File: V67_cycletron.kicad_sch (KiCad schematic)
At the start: 52 parts, among them J1 USB_C_Receptacle_USB2.0_16P, J3 Screw_Terminal_01x11, U1 LM1117DT-5.0, U2 LM1117DT-3.3, U4 ESP32-S3-WROOM-1

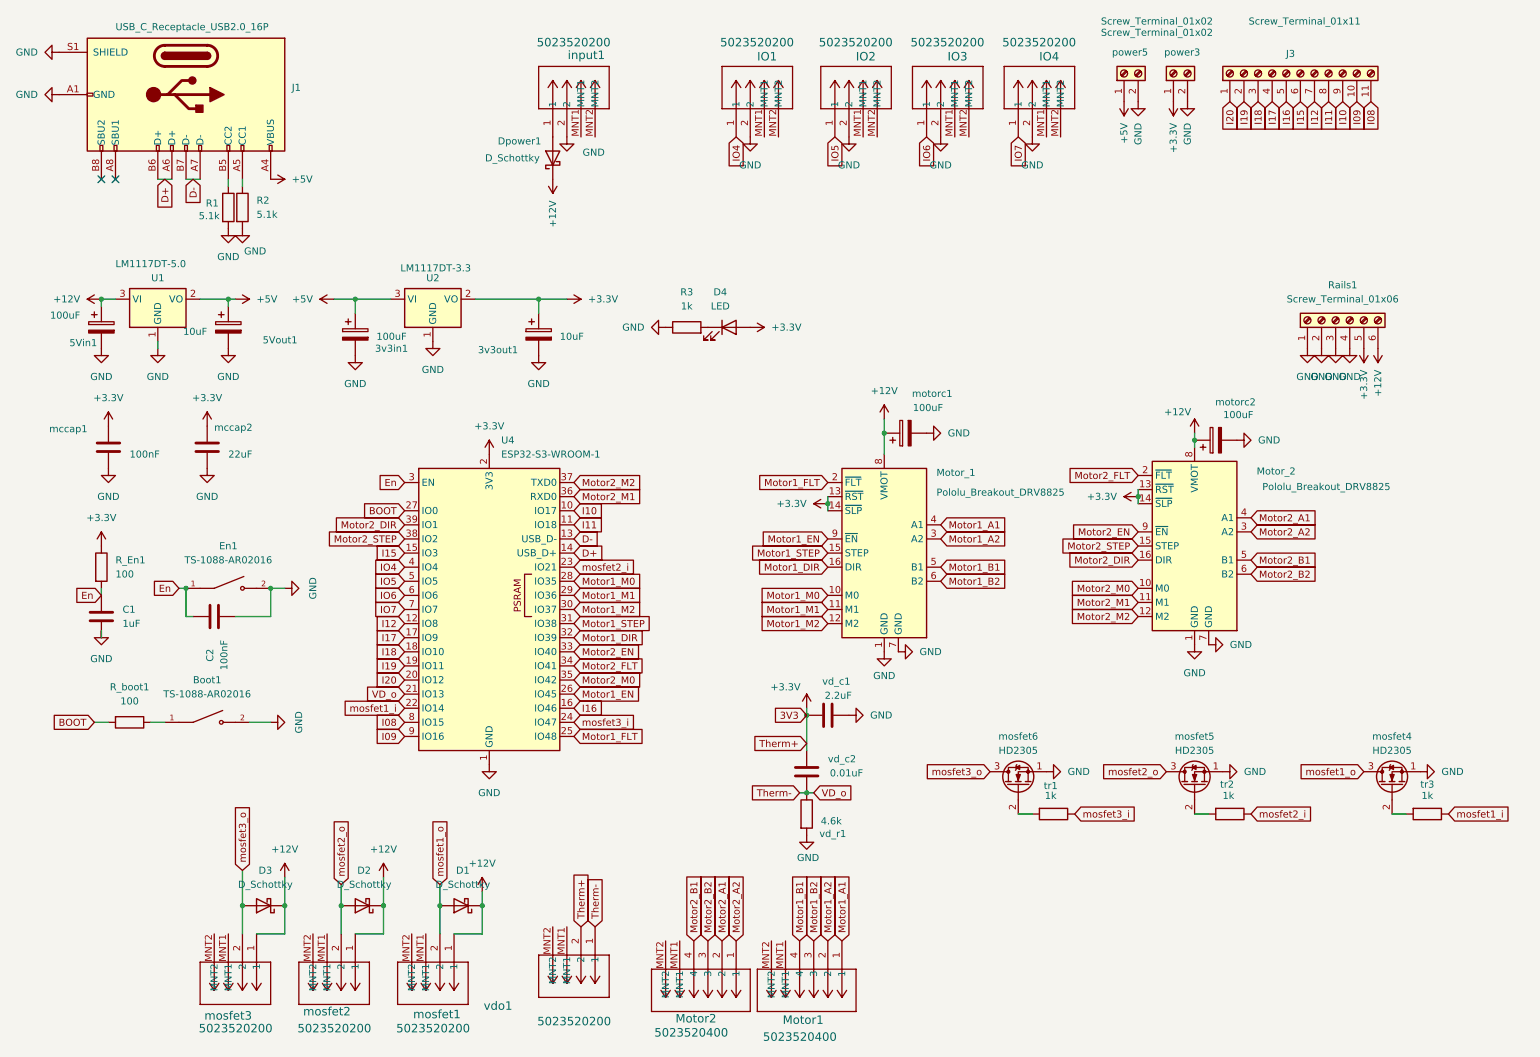
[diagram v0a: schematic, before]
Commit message: re-arranged connector positions
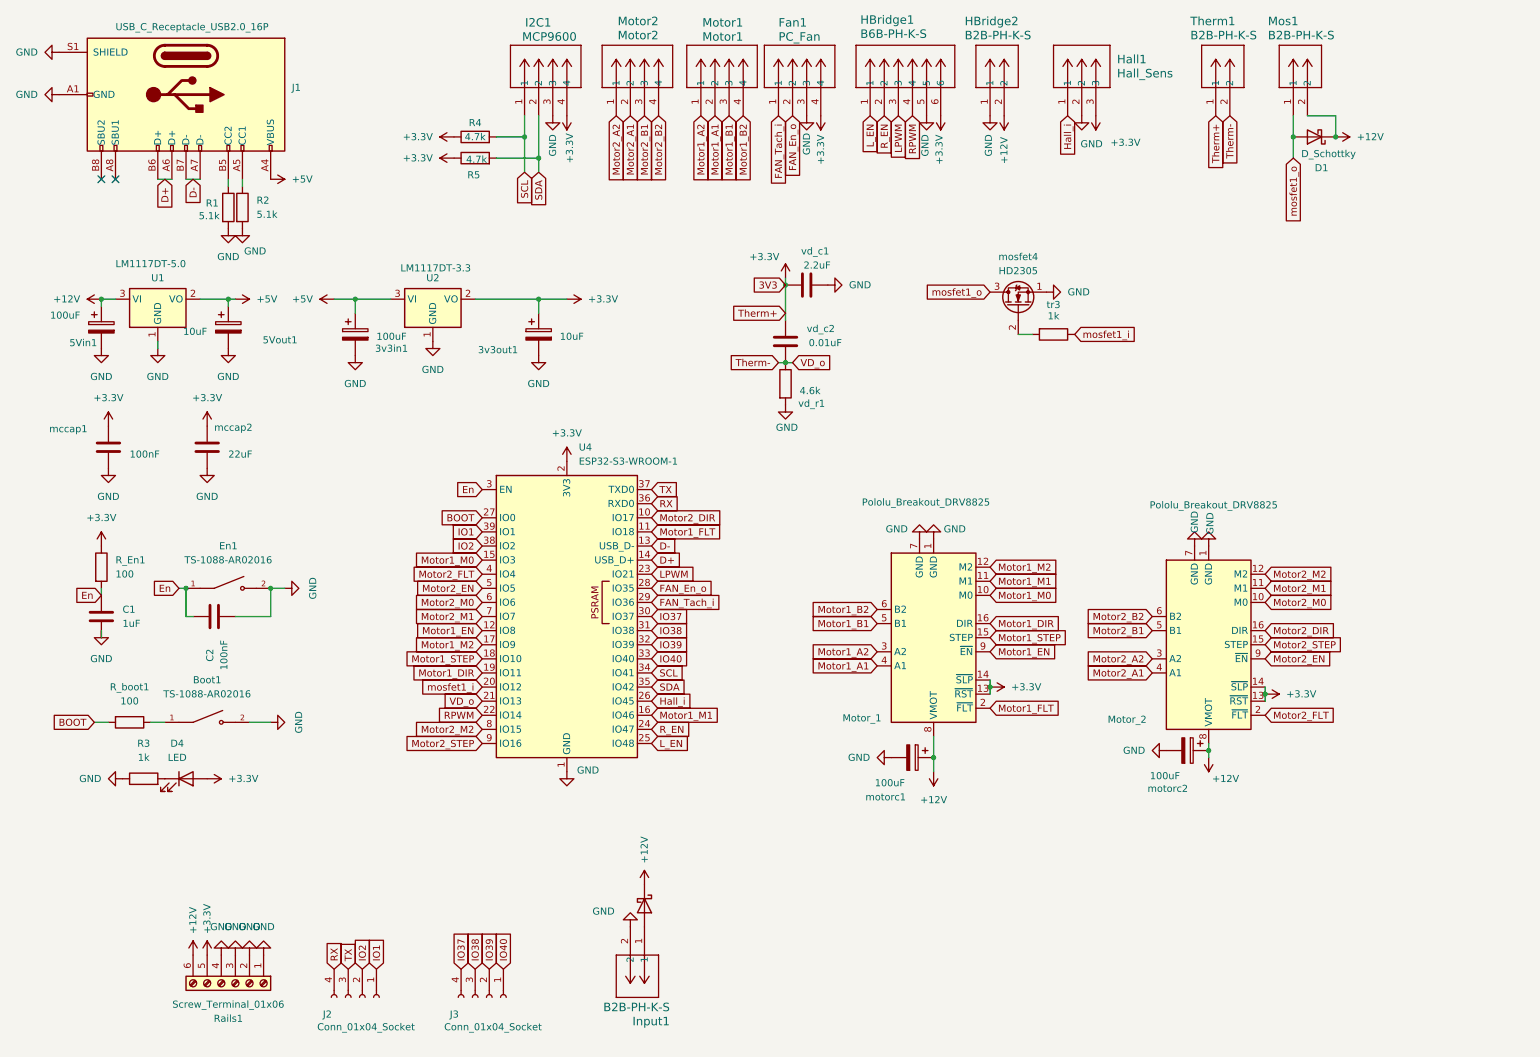
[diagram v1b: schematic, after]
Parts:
- removed D2, D3: D_Schottky, Diode_SMD:D_SMA, symbol Device:D_Schottky
- removed IO1, IO2, IO3, IO4, input1, mosfet1, mosfet2, mosfet3, vdo1: 5023520200, Connector_4:CONN_SD-502352-001_02_MOL, symbol Connector_2:5023520200
- removed J3: Screw_Terminal_01x11, TerminalBlock:TerminalBlock_MaiXu_MX126-5.0-11P_1x11_P5.00mm, symbol Connector:Screw_Terminal_01x11
- removed Motor1, Motor2: 5023520400, Connector_4:CONN_SD-502352-001_04_MOL, symbol Connector_4:5023520400
- removed mosfet5, mosfet6: HD2305, Package_TO_SOT_SMD:SOT-23, symbol Transistor_FET:2N7000
- removed power3, power5: Screw_Terminal_01x02, TerminalBlock:TerminalBlock_MaiXu_MX126-5.0-02P_1x02_P5.00mm, symbol Connector:Screw_Terminal_01x02
- removed tr1, tr2: 1k, Resistor_SMD:R_0805_2012Metric_Pad1.20x1.40mm_HandSolder, symbol Device:R
- added Fan1: PC_Fan, CONN4_B4B-PH_JST, symbol connector_4_new:B4B-PH-K-S
- added HBridge1: B6B-PH-K-S, connector_6_vert:CONN_B6B-PH-K-S_JST, symbol connector_6_new:B6B-PH-K-S
- added HBridge2, Input1, Mos1, Therm1: B2B-PH-K-S, connector_2_vert:CONN2_B2B-PH-K-S_JST, symbol connector_2_new:B2B-PH-K-S
- added Hall1: Hall_Sens, CONN_B3B-PH-K-SLFSN_JST, symbol connector_2_new:B3B-PH-K-SLFSN
- added I2C1: MCP9600, connector_4_vert:CONN4_B4B-PH_JST, symbol connector_4_new:B4B-PH-K-S
- added J2, J3: Conn_01x04_Socket, Connector_PinHeader_1.27mm:PinHeader_1x04_P1.27mm_Vertical, symbol Connector:Conn_01x04_Socket
- added Motor1: Motor1, CONN4_B4B-PH_JST, symbol connector_4_new:B4B-PH-K-S
- added Motor2: Motor2, CONN4_B4B-PH_JST, symbol connector_4_new:B4B-PH-K-S
- added R4, R5: 4.7k, Resistor_SMD:R_0805_2012Metric_Pad1.20x1.40mm_HandSolder, symbol Device:R
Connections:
- net I08 is gone; now on net Motor2_M2: U4.8 (IO15)
- net I09 is gone; now on net Motor2_STEP: U4.9 (IO16)
- net I10 is gone; now on net Motor2_DIR: U4.10 (IO17)
- net I11 is gone; now on net Motor1_FLT: U4.11 (IO18)
- net I12 is gone; now on net Motor1_EN: U4.12 (IO8)
- net I15 is gone; now on net Motor1_M0: U4.15 (IO3)
- net I16 is gone; now on net Motor1_M1: U4.16 (IO46)
- net I17 is gone; now on net Motor1_M2: U4.17 (IO9)
- net I18 is gone; now on net Motor1_STEP: U4.18 (IO10)
- net I19 is gone; now on net Motor1_DIR: U4.19 (IO11)
- net I20 is gone; now on net mosfet1_i: U4.20 (IO12)
- net IO4 is gone; now on net Motor2_FLT: U4.4 (IO4)
- net IO5 is gone; now on net Motor2_EN: U4.5 (IO5)
- net IO6 is gone; now on net Motor2_M0: U4.6 (IO6)
- net IO7 is gone; now on net Motor2_M1: U4.7 (IO7)
- net +12V: now also HBridge2.2, Mos1.2
- net +3.3V: now also Fan1.4, HBridge1.6, Hall1.3, I2C1.4, R4.1, R5.1, Therm1.1
- net GND: now also Fan1.3, HBridge1.5, HBridge2.1, Hall1.2, I2C1.3, Input1.2
- net Motor1_A1: now also Motor1.2
- net Motor1_A2: now also Motor1.1
- net Motor1_B1: now also Motor1.3
- net Motor1_B2: now also Motor1.4
- net Motor1_DIR: no longer U4.32 (IO39)
- net Motor1_EN: no longer U4.26 (IO45)
- net Motor1_FLT: no longer U4.25 (IO48)
- net Motor1_M0: no longer U4.28 (IO35)
- net Motor1_M1: no longer U4.29 (IO36)
- net Motor1_M2: no longer U4.30 (IO37)
- net Motor1_STEP: no longer U4.31 (IO38)
- net Motor2_A1: now also Motor2.2
- net Motor2_A2: now also Motor2.1
- net Motor2_B1: now also Motor2.3
- net Motor2_B2: now also Motor2.4
- net Motor2_DIR: no longer U4.39 (IO1)
- net Motor2_EN: no longer U4.33 (IO40)
- net Motor2_FLT: no longer U4.34 (IO41)
- net Motor2_M0: no longer U4.35 (IO42)
- net Motor2_M1: no longer U4.36 (RXD0)
- net Motor2_M2: no longer U4.37 (TXD0)
- net Motor2_STEP: no longer U4.38 (IO2)
- net Therm-: now also Therm1.2
- net mosfet1_i: no longer U4.22 (IO14)
- net mosfet1_o: now also Mos1.1
- net at Dpower1.2 (A): now also Input1.1
- net mosfet2_i renamed LPWM
- net LPWM: now also HBridge1.3
- net mosfet3_i renamed R_EN
- net R_EN: now also HBridge1.2
- new net FAN_En_o: Fan1.2, U4.28 (IO35)
- new net FAN_Tach_i: Fan1.1, U4.29 (IO36)
- new net Hall_i: Hall1.1, U4.26 (IO45)
- new net IO1: J2.1 (Pin_1), U4.39 (IO1)
- new net IO2: J2.2 (Pin_2), U4.38 (IO2)
- new net IO37: J3.4 (Pin_4), U4.30 (IO37)
- new net IO38: J3.3 (Pin_3), U4.31 (IO38)
- new net IO39: J3.2 (Pin_2), U4.32 (IO39)
- new net IO40: J3.1 (Pin_1), U4.33 (IO40)
- new net L_EN: HBridge1.1, U4.25 (IO48)
- new net RPWM: HBridge1.4, U4.22 (IO14)
- new net RX: J2.4 (Pin_4), U4.36 (RXD0)
- new net SCL: I2C1.1, R4.2, U4.34 (IO41)
- new net SDA: I2C1.2, R5.2, U4.35 (IO42)
- new net TX: J2.3 (Pin_3), U4.37 (TXD0)
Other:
- moved on the sheet: D1, D4, Motor_1, Motor_2, R3, Rails1, U4, mosfet4, motorc1, motorc2, tr3, vd_c1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

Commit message: edits to part selection, new regulator
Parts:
- removed U1: LM1117DT-5.0, Package_TO_SOT_SMD:TO-252-3_TabPin2, symbol Regulator_Linear:AMS1117-5.0
- added D5: LED, LED_SMD:LED_0603_1608Metric_Pad1.05x0.95mm_HandSolder, symbol Device:LED
- added R6: 1k, Resistor_SMD:R_0805_2012Metric_Pad1.20x1.40mm_HandSolder, symbol Device:R
- added R7: 4.7k, Resistor_SMD:R_0805_2012Metric_Pad1.20x1.40mm_HandSolder, symbol Device:R
- added U3: L7805, regulator_5V:TO255P460X1020X2008-3P, symbol Regulator_Linear:L7805
- added hall_cap1: 100nF, Capacitor_SMD:C_0805_2012Metric_Pad1.18x1.45mm_HandSolder, symbol Device:C
- HBridge1: footprint connector_6_vert:CONN_B6B-PH-K-S_JST -> connector_6_vert:JST_B6B-PH-K-S
- HBridge2, Input1, Mos1, Therm1: footprint connector_2_vert:CONN2_B2B-PH-K-S_JST -> connector_2_vert:JST_B2B-PH-K-S
- vd_r1: value 4.6k -> 4.7k
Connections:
- net +3.3V: now also HBridge1.5, R7.1, hall_cap1.2; no longer Fan1.4, HBridge1.6
- net +5V: now also U3.3 (OUT)
- net FAN_Tach_i: now also R7.2
- net GND: now also HBridge1.6, R6.1, U3.2 (GND), hall_cap1.1; no longer HBridge1.5
- net LPWM: now also HBridge1.2, U4.24 (IO47); no longer HBridge1.3, U4.23 (IO21)
- net L_EN: now also HBridge1.4, U4.22 (IO14); no longer HBridge1.1, U4.25 (IO48)
- net RPWM: now also HBridge1.1, U4.25 (IO48); no longer HBridge1.4, U4.22 (IO14)
- net R_EN: now also HBridge1.3, U4.23 (IO21); no longer HBridge1.2, U4.24 (IO47)
- net 24V_unsafe: now reaches Dpower1.2 (A), Input1.1
- net 24V_unsafe: now also D5.2 (A)
- net +12V renamed +24V
- net +24V: now also Fan1.4, U3.1 (IN)
- new net: D5.1 (K), R6.2
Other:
- moved on the sheet: vd_c1, vd_c2, vd_r1

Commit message: push after order
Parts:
- renumbered hall_cap1 to hall2, HBridge1 to hb1, HBridge2 to hb2
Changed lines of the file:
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@@
 		(on_board yes)
 		(dnp no)
-		(property "Reference" "hall_cap1"
-			(at 213.868 32.004 90)
+		(property "Reference" "hall2"
+			(at 211.328 32.004 90)
 			(effects
 				(font
@@
 			(project "V67_cycletron"
 				(path "/490d8b32-3aea-4f11-93e7-a546853a1b13"
-					(reference "hall_cap1")
+					(reference "hall2")
 					(unit 1)
 				)
@@
 		(on_board yes)
 		(dnp no)
-		(property "Reference" "HBridge1"
+		(property "Reference" "hb1"
 			(at 165.862 13.208 90)
 			(effects
@@
 			(project ""
 				(path "/490d8b32-3aea-4f11-93e7-a546853a1b13"
-					(reference "HBridge1")
+					(reference "hb1")
 					(unit 1)
 				)
@@
 		(on_board yes)
 		(dnp no)
-		(property "Reference" "HBridge2"
+		(property "Reference" "hb2"
 			(at 184.658 13.462 90)
 			(effects
@@
 			(project ""
 				(path "/490d8b32-3aea-4f11-93e7-a546853a1b13"
-					(reference "HBridge2")
+					(reference "hb2")
 					(unit 1)
 				)

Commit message: changed usb-c connector part LCSC number for manufuactering
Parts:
- J1: LCSC C5338271 -> C5337088
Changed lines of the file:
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@@
 			)
 		)
-		(property "LCSC" "C5338271"
+		(property "LCSC" "C5337088"
 			(at 63.5 25.3999 0)
 			(effects
